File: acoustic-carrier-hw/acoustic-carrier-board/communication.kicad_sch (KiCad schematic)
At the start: 55 parts, among them IC1 ECP5-BGA256, J9 HR911130A, U1 KSZ9031RN, Y1 25MHz

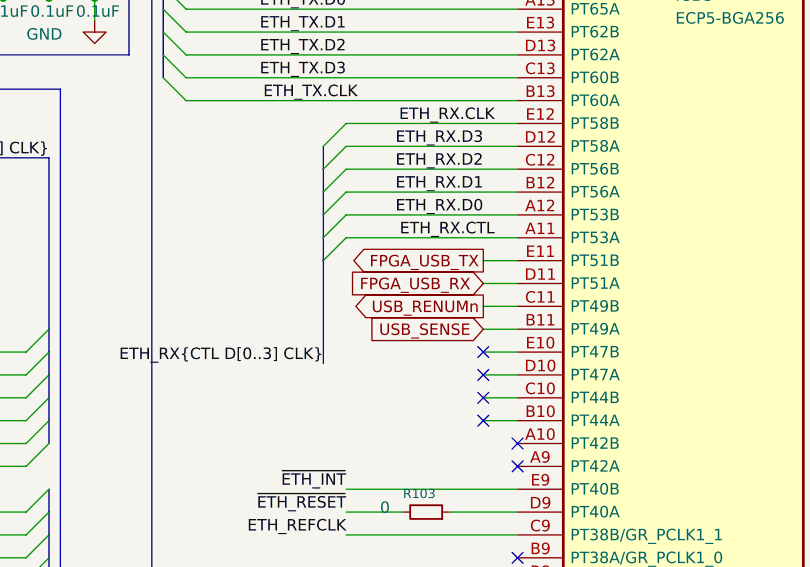
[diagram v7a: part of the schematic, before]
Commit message: [carrier] Doing schmitt trigger calculations and simulations, choosing comparator, choosing USB connector
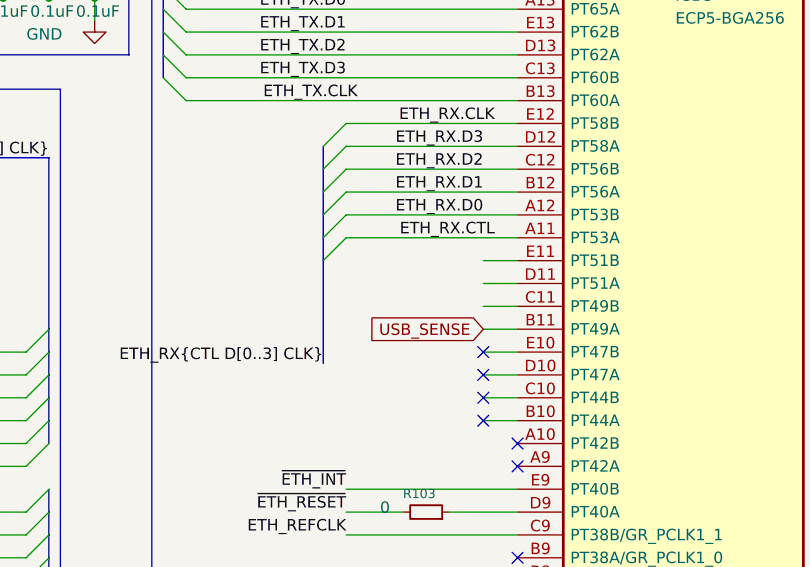
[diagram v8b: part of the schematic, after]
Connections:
- net FPGA_USB_RX: no longer names the net of IC1.D11 (PT51A)
- net FPGA_USB_TX: no longer names the net of IC1.E11 (PT51B)
- net USB_RENUMn: no longer names the net of IC1.C11 (PT49B)
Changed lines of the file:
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@@
-		)
-	)
-	(global_label "FPGA_USB_RX"
-		(shape input)
-		(at 242.57 72.39 180)
-		(fields_autoplaced yes)
-		(effects
-			(font
-				(size 1.27 1.27)
-			)
-			(justify right)
-		)
-		(property "Intersheetrefs" "${INTERSHEET_REFS}"
-			(at 226.6429 72.39 0)
-			(effects
-				(font
-					(size 1.27 1.27)
-				)
-				(justify right)
-				(hide yes)
-			)
 		)
 	)
@@
 				)
 				(justify left)
-				(hide yes)
-			)
-		)
-	)
-	(global_label "USB_RENUMn"
-		(shape output)
-		(at 242.57 74.93 180)
-		(fields_autoplaced yes)
-		(effects
-			(font
-				(size 1.27 1.27)
-			)
-			(justify right)
-		)
-		(property "Intersheetrefs" "${INTERSHEET_REFS}"
-			(at 227.1268 74.93 0)
-			(effects
-				(font
-					(size 1.27 1.27)
-				)
-				(justify right)
 				(hide yes)
 			)
@@
 			(effects
 				(font
-					(size 1.27 1.27)
-				)
-				(justify right)
-				(hide yes)
-			)
-		)
-	)
-	(global_label "FPGA_USB_TX"
-		(shape output)
-		(at 242.57 69.85 180)
-		(fields_autoplaced yes)
-		(effects
-			(font
-				(size 1.27 1.27)
-			)
-			(justify right)
-		)
-		(property "Intersheetrefs" "${INTERSHEET_REFS}"
-			(at 226.9453 69.85 0)
-			(effects
-				(font
